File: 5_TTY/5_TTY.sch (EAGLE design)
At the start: 26 parts, among them Q2 BC857C, Q3 BC857C, Q4 BC857C, Q5 BC857C, Q6 BC857C, T4 BC847, X11 ALLSERIALD, X7 AKL18X-04W

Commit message: new BOMs,
finish TTY board
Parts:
- removed SV5: (no value), con-ml:ML14L
- added R1, R2: 33R, resistor:R-EU_R0805
- added SV1: (no value), con-lstb:MA08-2W
- R18: value 10k -> 180k
- R20: value 1k -> 4k7
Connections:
- new net CS1: R1.1, SV1.3
- new net CS2: R2.1, SV1.4
- net +12V: now also SV1.1, SV1.2
- net CC1: now also SV1.15; no longer SV5.13
- net CC2: now also SV1.16; no longer SV5.14
- net GND: now also R18.2, SV1.10, SV1.9; no longer SV5.7, SV5.8
- net N$44: now also SV1.11, X7-2.S; no longer SV5.9
- net N$46: no longer R18.2
- net N$49: now also R2.2
- net N$59: now also R1.2
- net N$65: now also SV1.12, X7-4.S; no longer SV5.10
- net RXN: now also SV1.7, X7-3.S; no longer SV5.5
- net RXP: now also SV1.14, SV1.6; no longer SV5.12, SV5.4
- net TXN: now also SV1.8, X7-1.S; no longer SV5.6
- net TXP: now also SV1.13, SV1.5; no longer SV5.11, SV5.3
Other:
- note added: "40 mA RX"
- note added: "40 mA TX"
- moved on the sheet: Q2, Q3, Q4, Q6, R14, R15, R16, R17, R18, R20, X7-1, X7-2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

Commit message: add author
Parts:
- renumbered SV1 to X2, X11 to X1
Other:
- note added: "Seegel Systeme Königstraße 57 90762 Fürth www.seegel-systeme.de post@seegel-systeme.de +49 (911) / 8915295"
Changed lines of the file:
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@@
 <?xml version="1.0" encoding="utf-8"?>
 <!DOCTYPE eagle SYSTEM "eagle.dtd">
-<eagle version="7.6.0">
+<eagle version="7.7.0">
 <drawing>
 <settings>
@@
 <attribute name="FARNELL" value="2498050"/>
 </part>
-<part name="X11" library="AllSerial" deviceset="ALLSERIAL" device="D"/>
+<part name="X1" library="AllSerial" deviceset="ALLSERIAL" device="D"/>
 <part name="GND1" library="supply1" deviceset="GND" device=""/>
 <part name="GND2" library="supply1" deviceset="GND" device=""/>
@@
 <part name="P+5" library="supply1" deviceset="+12V" device=""/>
 <part name="P+6" library="supply1" deviceset="+12V" device=""/>
-<part name="SV1" library="con-lstb" deviceset="MA08-2W" device=""/>
+<part name="X2" library="con-lstb" deviceset="MA08-2W" device=""/>
 <part name="R1" library="resistor" deviceset="R-EU_" device="R0805" value="33R">
 <attribute name="FARNELL" value="2498090"/>
@@
 <text x="195.58" y="70.358" size="1.778" layer="94">40 mA TX</text>
 <text x="195.58" y="67.564" size="1.778" layer="94">40 mA RX</text>
+<text x="165.1" y="7.62" size="1.778" layer="94">Seegel Systeme
+Königstraße 57
+90762 Fürth
+www.seegel-systeme.de
+post@seegel-systeme.de
++49 (911) / 8915295</text>
 </plain>
 <instances>
@@
 <attribute name="FARNELL" x="83.82" y="68.58" size="1.778" layer="96" rot="R90" display="off"/>
 </instance>
-<instance part="X11" gate="DAT" x="22.86" y="83.82"/>
-<instance part="X11" gate="PWR" x="22.86" y="35.56"/>
+<instance part="X1" gate="DAT" x="22.86" y="83.82"/>
+<instance part="X1" gate="PWR" x="22.86" y="35.56"/>
 <instance part="GND1" gate="1" x="22.86" y="15.24"/>
 <instance part="GND2" gate="1" x="15.24" y="114.3"/>
@@
 <instance part="P+5" gate="1" x="22.86" y="162.56"/>
 <instance part="P+6" gate="1" x="50.8" y="162.56"/>
-<instance part="SV1" gate="1" x="177.8" y="127" rot="R90"/>
+<instance part="X2" gate="1" x="177.8" y="127" rot="R90"/>
 <instance part="R1" gate="G$1" x="33.02" y="147.32" smashed="yes" rot="R270">
 <attribute name="NAME" x="35.052" y="147.2946" size="1.778" layer="95"/>
@@
 <wire x1="154.94" y1="111.76" x2="177.8" y2="111.76" width="0.1524" layer="91"/>
 <wire x1="177.8" y1="111.76" x2="177.8" y2="119.38" width="0.1524" layer="91"/>
-<pinref part="SV1" gate="1" pin="8"/>
+<pinref part="X2" gate="1" pin="8"/>
 <wire x1="154.94" y1="147.32" x2="203.2" y2="147.32" width="0.1524" layer="91"/>
 <wire x1="154.94" y1="147.32" x2="154.94" y2="111.76" width="0.1524" layer="91"/>
@@
 <wire x1="180.34" y1="137.16" x2="180.34" y2="134.62" width="0.1524" layer="91"/>
 <junction x="170.18" y="137.16"/>
-<pinref part="SV1" gate="1" pin="5"/>
-<pinref part="SV1" gate="1" pin="13"/>
+<pinref part="X2" gate="1" pin="5"/>
+<pinref part="X2" gate="1" pin="13"/>
 </segment>
 </net>
@@
 <wire x1="167.64" y1="134.62" x2="167.64" y2="137.16" width="0.1524" layer="91"/>
 <label x="167.64" y="137.16" size="1.27" layer="95" rot="R180" xref="yes"/>
-<pinref part="SV1" gate="1" pin="15"/>
+<pinref part="X2" gate="1" pin="15"/>
 </segment>
 </net>
@@
 <wire x1="167.64" y1="119.38" x2="167.64" y2="116.84" width="0.1524" layer="91"/>
 <label x="167.64" y="116.84" size="1.27" layer="95" rot="R180" xref="yes"/>
-<pinref part="SV1" gate="1" pin="16"/>
+<pinref part="X2" gate="1" pin="16"/>
 </segment>
 </net>
@@
 <wire x1="180.34" y1="116.84" x2="180.34" y2="119.38" width="0.1524" layer="91"/>
 <junction x="170.18" y="116.84"/>
-<pinref part="SV1" gate="1" pin="6"/>
-<pinref part="SV1" gate="1" pin="14"/>
+<pinref part="X2" gate="1" pin="6"/>
+<pinref part="X2" gate="1" pin="14"/>
 </segment>
 </net>
@@
 <wire x1="177.8" y1="142.24" x2="203.2" y2="142.24" width="0.1524" layer="91"/>
 <junction x="177.8" y="142.24"/>
-<pinref part="SV1" gate="1" pin="7"/>
+<pinref part="X2" gate="1" pin="7"/>
 <pinref part="X7" gate="-3" pin="S"/>
 </segment>
@@
 <wire x1="83.82" y1="76.2" x2="68.58" y2="76.2" width="0.1524" layer="91"/>
 <wire x1="68.58" y1="76.2" x2="68.58" y2="96.52" width="0.1524" layer="91"/>
-<pinref part="X11" gate="DAT" pin="RXD"/>
+<pinref part="X1" gate="DAT" pin="RXD"/>
 <wire x1="68.58" y1="96.52" x2="33.02" y2="96.52" width="0.1524" layer="91"/>
 </segment>
@@
 <wire x1="172.72" y1="134.62" x2="172.72" y2="144.78" width="0.1524" layer="91"/>
 <wire x1="172.72" y1="144.78" x2="203.2" y2="144.78" width="0.1524" layer="91"/>
-<pinref part="SV1" gate="1" pin="11"/>
+<pinref part="X2" gate="1" pin="11"/>
 <pinref part="X7" gate="-2" pin="S"/>
 </segment>
@@
 <wire x1="172.72" y1="119.38" x2="172.72" y2="106.68" width="0.1524" layer="91"/>
 <wire x1="172.72" y1="106.68" x2="198.12" y2="106.68" width="0.1524" layer="91"/>
-<pinref part="SV1" gate="1" pin="12"/>
+<pinref part="X2" gate="1" pin="12"/>
 <wire x1="198.12" y1="106.68" x2="198.12" y2="139.7" width="0.1524" layer="91"/>
 <pinref part="X7" gate="-4" pin="S"/>
@@
 <net name="N$91" class="0">
 <segment>
-<pinref part="X11" gate="DAT" pin="TXD"/>
+<pinref part="X1" gate="DAT" pin="TXD"/>
 <wire x1="33.02" y1="99.06" x2="68.58" y2="99.06" width="0.1524" layer="91"/>
 <wire x1="68.58" y1="99.06" x2="68.58" y2="137.16" width="0.1524" layer="91"/>
@@
 <net name="GND" class="0">
 <segment>
-<pinref part="X11" gate="PWR" pin="GND"/>
+<pinref part="X1" gate="PWR" pin="GND"/>
 <wire x1="22.86" y1="17.78" x2="22.86" y2="20.32" width="0.1524" layer="91"/>
 <pinref part="GND1" gate="1" pin="GND"/>
@@
 <wire x1="175.26" y1="119.38" x2="175.26" y2="104.14" width="0.1524" layer="91"/>
 <pinref part="GND6" gate="1" pin="GND"/>
-<pinref part="SV1" gate="1" pin="10"/>
+<pinref part="X2" gate="1" pin="10"/>
 </segment>
 <segment>
 <wire x1="175.26" y1="134.62" x2="175.26" y2="152.4" width="0.1524" layer="91"/>
 <pinref part="GND7" gate="1" pin="GND"/>
-<pinref part="SV1" gate="1" pin="9"/>
+<pinref part="X2" gate="1" pin="9"/>
 </segment>
 <segment>
@@
 <net name="+5V" class="0">
 <segment>
-<pinref part="X11" gate="PWR" pin="VIN"/>
+<pinref part="X1" gate="PWR" pin="VIN"/>
 <wire x1="33.02" y1="45.72" x2="38.1" y2="45.72" width="0.1524" layer="91"/>
 <wire x1="38.1" y1="45.72" x2="38.1" y2="50.8" width="0.1524" layer="91"/>
-<pinref part="X11" gate="PWR" pin="+5V"/>
+<pinref part="X1" gate="PWR" pin="+5V"/>
 <wire x1="33.02" y1="38.1" x2="38.1" y2="38.1" width="0.1524" layer="91"/>
 <wire x1="38.1" y1="38.1" x2="38.1" y2="45.72" width="0.1524" layer="91"/>
@@
 <net name="+12V" class="0">
 <segment>
-<pinref part="X11" gate="PWR" pin="+12V"/>
+<pinref part="X1" gate="PWR" pin="+12V"/>
 <wire x1="33.02" y1="40.64" x2="48.26" y2="40.64" width="0.1524" layer="91"/>
 <wire x1="48.26" y1="40.64" x2="48.26" y2="50.8" width="0.1524" layer="91"/>
@@
 </segment>
 <segment>
-<pinref part="SV1" gate="1" pin="1"/>
+<pinref part="X2" gate="1" pin="1"/>
 <wire x1="185.42" y1="134.62" x2="185.42" y2="137.16" width="0.1524" layer="91"/>
 <wire x1="185.42" y1="137.16" x2="190.5" y2="137.16" width="0.1524" layer="91"/>
 <wire x1="190.5" y1="137.16" x2="190.5" y2="127" width="0.1524" layer="91"/>
-<pinref part="SV1" gate="1" pin="2"/>
+<pinref part="X2" gate="1" pin="2"/>
 <wire x1="190.5" y1="127" x2="190.5" y2="116.84" width="0.1524" layer="91"/>
 <wire x1="190.5" y1="116.84" x2="185.42" y2="116.84" width="0.1524" layer="91"/>
@@
 </segment>
 <segment>
-<pinref part="SV1" gate="1" pin="3"/>
+<pinref part="X2" gate="1" pin="3"/>
 <wire x1="182.88" y1="134.62" x2="182.88" y2="139.7" width="0.1524" layer="91"/>
 <wire x1="182.88" y1="139.7" x2="185.42" y2="139.7" width="0.1524" layer="91"/>
@@
 </segment>
 <segment>
-<pinref part="SV1" gate="1" pin="4"/>
+<pinref part="X2" gate="1" pin="4"/>
 <wire x1="182.88" y1="119.38" x2="182.88" y2="114.3" width="0.1524" layer="91"/>
 <wire x1="182.88" y1="114.3" x2="185.42" y2="114.3" width="0.1524" layer="91"/>

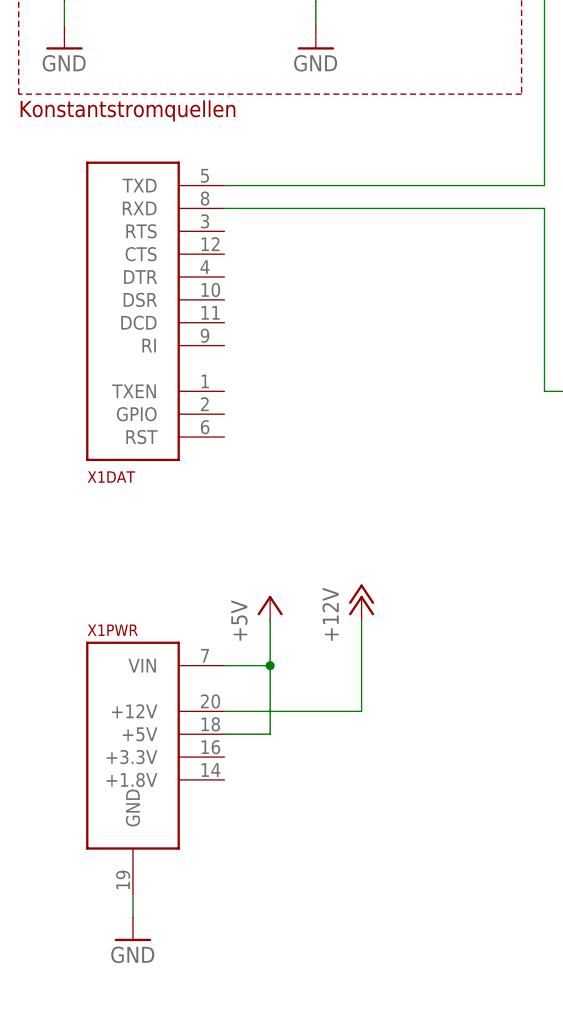
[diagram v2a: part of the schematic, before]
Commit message: change to libv2
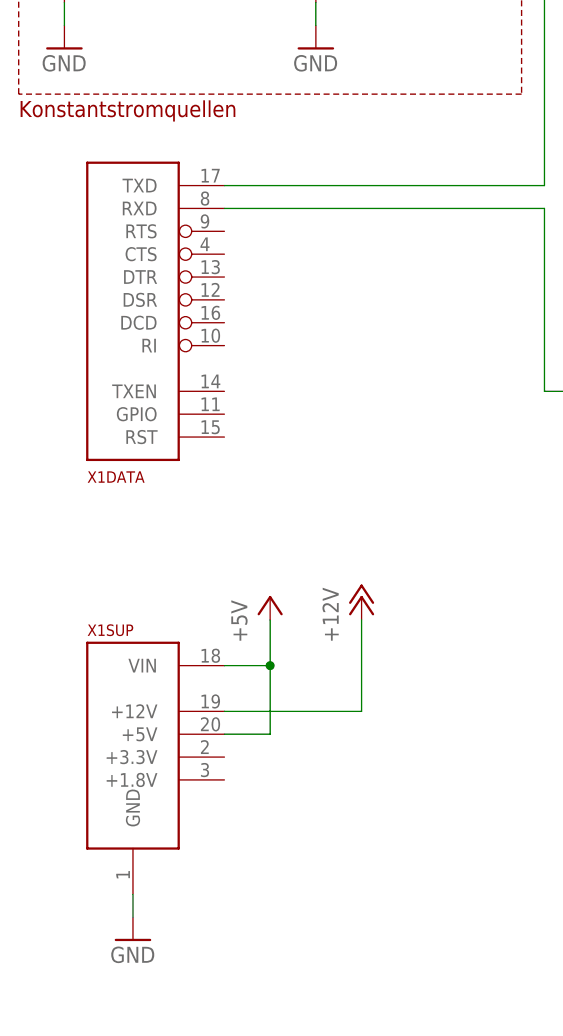
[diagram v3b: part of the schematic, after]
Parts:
- X1: value ALLSERIALD -> ALLSERIALSLAVE; device AllSerial:ALLSERIALD -> AllSerialv2:ALLSERIALSLAVE
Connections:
- net +12V: now also X1SUP.+12V; no longer X1PWR.+12V
- net +5V: now also X1SUP.+5V, X1SUP.VIN; no longer X1PWR.+5V, X1PWR.VIN
- net GND: now also X1SUP.GND; no longer X1PWR.GND
- net N$46: now also X1DATA.RXD; no longer X1DAT.RXD
- net N$91: now also X1DATA.TXD; no longer X1DAT.TXD
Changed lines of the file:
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@@
 <?xml version="1.0" encoding="utf-8"?>
 <!DOCTYPE eagle SYSTEM "eagle.dtd">
-<eagle version="7.7.0">
+<eagle version="7.6.0">
 <drawing>
 <settings>
@@
 <attribute name="FARNELL" value="2498050"/>
 </part>
-<part name="X1" library="AllSerial" deviceset="ALLSERIAL" device="D"/>
 <part name="GND1" library="supply1" deviceset="GND" device=""/>
 <part name="GND2" library="supply1" deviceset="GND" device=""/>
@@
 <part name="P+7" library="supply1" deviceset="+12V" device=""/>
 <part name="GND8" library="supply1" deviceset="GND" device=""/>
+<part name="X1" library="AllSerialv2" deviceset="ALLSERIALSLAVE" device=""/>
 </parts>
 <sheets>
@@
 <attribute name="FARNELL" x="83.82" y="68.58" size="1.778" layer="96" rot="R90" display="off"/>
 </instance>
-<instance part="X1" gate="DAT" x="22.86" y="83.82"/>
-<instance part="X1" gate="PWR" x="22.86" y="35.56"/>
 <instance part="GND1" gate="1" x="22.86" y="15.24"/>
 <instance part="GND2" gate="1" x="15.24" y="114.3"/>
@@
 <instance part="P+7" gate="1" x="195.58" y="127" rot="R270"/>
 <instance part="GND8" gate="1" x="91.44" y="58.42"/>
+<instance part="X1" gate="DATA" x="22.86" y="83.82"/>
+<instance part="X1" gate="SUP" x="22.86" y="35.56"/>
 </instances>
 <busses>
@@
 <wire x1="83.82" y1="76.2" x2="68.58" y2="76.2" width="0.1524" layer="91"/>
 <wire x1="68.58" y1="76.2" x2="68.58" y2="96.52" width="0.1524" layer="91"/>
-<pinref part="X1" gate="DAT" pin="RXD"/>
 <wire x1="68.58" y1="96.52" x2="33.02" y2="96.52" width="0.1524" layer="91"/>
+<pinref part="X1" gate="DATA" pin="RXD"/>
 </segment>
 </net>
@@
 <net name="N$91" class="0">
 <segment>
-<pinref part="X1" gate="DAT" pin="TXD"/>
 <wire x1="33.02" y1="99.06" x2="68.58" y2="99.06" width="0.1524" layer="91"/>
 <wire x1="68.58" y1="99.06" x2="68.58" y2="137.16" width="0.1524" layer="91"/>
 <pinref part="Q5" gate="G$1" pin="B"/>
 <wire x1="68.58" y1="137.16" x2="78.74" y2="137.16" width="0.1524" layer="91"/>
+<pinref part="X1" gate="DATA" pin="TXD"/>
 </segment>
 </net>
 <net name="GND" class="0">
 <segment>
-<pinref part="X1" gate="PWR" pin="GND"/>
 <wire x1="22.86" y1="17.78" x2="22.86" y2="20.32" width="0.1524" layer="91"/>
 <pinref part="GND1" gate="1" pin="GND"/>
+<pinref part="X1" gate="SUP" pin="GND"/>
 </segment>
 <segment>
@@
 <net name="+5V" class="0">
 <segment>
-<pinref part="X1" gate="PWR" pin="VIN"/>
 <wire x1="33.02" y1="45.72" x2="38.1" y2="45.72" width="0.1524" layer="91"/>
 <wire x1="38.1" y1="45.72" x2="38.1" y2="50.8" width="0.1524" layer="91"/>
-<pinref part="X1" gate="PWR" pin="+5V"/>
 <wire x1="33.02" y1="38.1" x2="38.1" y2="38.1" width="0.1524" layer="91"/>
 <wire x1="38.1" y1="38.1" x2="38.1" y2="45.72" width="0.1524" layer="91"/>
 <junction x="38.1" y="45.72"/>
 <pinref part="P+2" gate="1" pin="+5V"/>
+<pinref part="X1" gate="SUP" pin="+5V"/>
+<pinref part="X1" gate="SUP" pin="VIN"/>
 </segment>
 <segment>
@@
 <net name="+12V" class="0">
 <segment>
-<pinref part="X1" gate="PWR" pin="+12V"/>
 <wire x1="33.02" y1="40.64" x2="48.26" y2="40.64" width="0.1524" layer="91"/>
 <wire x1="48.26" y1="40.64" x2="48.26" y2="50.8" width="0.1524" layer="91"/>
 <pinref part="P+1" gate="1" pin="+12V"/>
-</segment>
-<segment>
+<pinref part="X1" gate="SUP" pin="+12V"/>
+</segment>
+<segment>

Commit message: final design & order
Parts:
- removed OK3: 4N25, optocoupler:4N35
- removed X7: AKL18X-04W, con-riacon_akl:AKL18X-04W
- added OK2: 4N25, optocoupler:4N35
- added R3, R4: 68R, resistor:R-EU_R0805
- added X3: MA03-2W, con-lstb:MA03-2W
- R1, R2: value 33R -> 15R
- R14: value 33R -> 68R
- X2: value (none) -> AKL18X-08W; device con-lstb:MA08-2W -> con-riacon_akl:AKL18X-08W
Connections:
- removed net CS1: R1.1, X2.3
- removed net CS2: R2.1, X2.4
- removed net N$44: X2.11, X7-2.S
- removed net N$65: X2.12, X7-4.S
- removed net RXN: D2.A, OK1.C, X2.7, X7-3.S
- removed net RXP: D2.C, R19.1, X2.14, X2.6
- removed net TXN: OK3.EMI, R11.2, T4.E, X2.8, X7-1.S
- new net N$2: R1.1, X3.2
- new net N$3: R2.1, X3.1
- new net N$4: OK2.EMI, R11.2, T4.E, X2-6.S
- new net N$5: R3.1, X3.6
- new net N$6: R4.1, X3.5
- new net N$7: D2.C, R19.1, X2-3.S
- new net N$8: D2.A, OK1.C, X2-2.S
- net +12V: now also X3.3, X3.4; no longer X2.1, X2.2
- net CC1: now also X2-4.S; no longer X2.15
- net CC2: now also X2-8.S; no longer X2.16
- net GND: now also OK2.C, X2-1.S, X2-5.S; no longer OK3.C, X2.10, X2.9
- net N$49: now also R4.2
- net N$54: now also OK2.BAS; no longer OK3.BAS
- net N$55: now also OK2.COL; no longer OK3.COL
- net N$59: now also R3.2
- net N$60: now also OK2.A; no longer OK3.A
- net TXP: now also X2-7.S; no longer X2.13, X2.5
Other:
- note added: "GND"
- note added: "RX+"
- note added: "RX-"
- note added: "TX+"
- note added: "TX-"
- note added: "V+"
- note removed: "2 wire active RXO/RXI"
- note removed: "2 wire passive TXO/RXI"
- note removed: "3 wire active (TXI = COM)"
- note removed: "3 wire active RX TXO = COM"
- note removed: "3 wire active TX RXO = COM"
- note removed: "3 wire passive (TXO = COM)"
- note removed: "4 wire active"
- note removed: "4 wire active RX"
- note removed: "4 wire active TX"
- note removed: "4 wire passive"
- note removed: "40 mA RX"
- note removed: "40 mA TX"
- note removed: "RXI"
- note removed: "RXO"
- note removed: "TXI"
- note removed: "TXO"
- moved on the sheet: D1, D2, LED5, LED6, OK1, Q2, Q3, Q4, Q5, Q6, R1, R10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
